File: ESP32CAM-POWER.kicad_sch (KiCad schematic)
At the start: 13 parts, among them J1 Conn_01x02_Female, J2 Conn_01x06_Male, U1 D-SUN-MP1584EN, U2 ESP32-CAM

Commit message: some chages for V1.3
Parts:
- added C1: 100nF, Capacitor_SMD:C_0603_1608Metric, symbol Device:C
- added D3: BZV55C5V1, Diode_SMD:D_MiniMELF, symbol Diode:BZV55C5V1
- added D5, D6, D7, D8: WS2812B, LED_SMD:LED_WS2812B_PLCC4_5.0x5.0mm_P3.2mm, symbol LED:WS2812B
- added J3: Conn_01x02_Male, Jumper:SolderJumper-2_P1.3mm_Open_RoundedPad1.0x1.5mm, symbol Connector:Conn_01x02_Male
- added R3: 10k, Resistor_SMD:R_0603_1608Metric, symbol Device:R
- added SW1: BOOT, Button_Switch_SMD:SW_Push_1P1T_NO_6x6mm_H9.5mm, symbol Switch:SW_SPST
- renumbered D2 to D1, D3 to D2, D1 to D4
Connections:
- net +5V: now also D3.1 (K), D5.1 (VDD), D6.1 (VDD), D7.1 (VDD), D8.1 (VDD), J3.2 (Pin_2); no longer U1.7 (VOUT+), U1.8 (VOUT+)
- net BOOT: now also C1.1, R3.2, SW1.2 (B); no longer J2.6 (Pin_6)
- net GND: now also J2.1 (Pin_1), C1.2, D3.2 (A), D5.3 (VSS), D6.3 (VSS), D7.3 (VSS), D8.3 (VSS), SW1.1 (A); no longer J2.4 (Pin_4), J2.5 (Pin_5)
- net RX: now also J2.4 (Pin_4); no longer J2.3 (Pin_3)
- net TX: now also J2.5 (Pin_5); no longer J2.2 (Pin_2)
- net at D4.2 (A): now also J2.3 (Pin_3); no longer J2.1 (Pin_1)
- net LED: now reaches U2.3 (IO12)
- net LED: now also D5.4 (DIN)
- net +3V3: now reaches U2.9 (3V3)
- net +3V3: now also R3.1
- new net: D6.2 (DOUT), D7.4 (DIN)
- new net: D5.2 (DOUT), D6.4 (DIN)
- new net: J3.1 (Pin_1), U1.7 (VOUT+), U1.8 (VOUT+)
- new net: D7.2 (DOUT), D8.4 (DIN)
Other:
- note added: "Adafruit FTDI Cable https://cdn-shop.adafruit.com/datasheets/FT232_Model.pdf 1: GND 2: CTS 3: 5V 4: TXD 3.3V 5: RXD 3.3V 6: RTS"
- note added: "https://raw.githubusercontent.com/SeeedDocument/forum_doc/master/reg/ESP32_CAM_V1.6.pdf"
- moved on the sheet: U2

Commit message: serveral changes, add USB, still a bit messy
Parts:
- removed C1: 100nF, Capacitor_SMD:C_0603_1608Metric, symbol Device:C
- removed D3: BZV55C5V1, Diode_SMD:D_MiniMELF, symbol Diode:BZV55C5V1
- removed D4: 1N4148WS, Diode_SMD:D_SOD-323, symbol Diode:1N4148WS
- removed J2: Conn_01x06_Male, Connector_PinHeader_2.54mm:PinHeader_1x06_P2.54mm_Horizontal, symbol Connector:Conn_01x06_Male
- removed J3: Conn_01x02_Male, Jumper:SolderJumper-2_P1.3mm_Open_RoundedPad1.0x1.5mm, symbol Connector:Conn_01x02_Male
- removed SW1: BOOT, Button_Switch_SMD:SW_Push_1P1T_NO_6x6mm_H9.5mm, symbol Switch:SW_SPST
- added C1, C2: 1uF, Capacitor_SMD:C_0603_1608Metric, symbol Device:C_Small
- added C3, C4: 20pF, Capacitor_SMD:C_0603_1608Metric, symbol Device:C_Small
- added D10, D9: 1N4148WS, Diode_SMD:D_SOD-323, symbol Diode:1N4148WS
- added D3: LED_O, LED_SMD:LED_0603_1608Metric, symbol Device:LED
- added D4: SN4001W, Diode_SMD:D_SOD-123, symbol Diode:SM4001
- added J2: USB_B_Micro, Connector_USB:USB_Micro-B_Amphenol_10118194_Horizontal, symbol Connector:USB_B_Micro
- added SW1: RESET, bouni:TS-1187A-B-A-B, symbol Switch:SW_DPST
- added SW2: BOOT, bouni:TS-1187A-B-A-B, symbol Switch:SW_DPST
- added TP1, TP2, TP3, TP4: TestPoint, TestPoint:TestPoint_Pad_D1.5mm, symbol Connector:TestPoint
- added U3: ME6206A33XG, Package_TO_SOT_SMD:SOT-23, symbol Regulator_Linear:LM3480-3.3
- added U4: CH340G, Package_SO:SOIC-16_3.9x9.9mm_P1.27mm, symbol Interface_USB:CH340G
- added Y1: 12Mhz, Crystal:Crystal_SMD_3225-4Pin_3.2x2.5mm, symbol Device:Crystal_GND24_Small
- D5, D6, D7, D8, H1, H2, H3, H4, U1, U2: now left out of the parts list
- J1: footprint Connector_Phoenix_MSTB:PhoenixContact_MSTBVA_2,5_2-G-5,08_1x02_P5.08mm_Vertical -> TerminalBlock_RND:TerminalBlock_RND_205-00232_1x02_P5.08mm_Horizontal; now left out of the parts list
- R2, R3: value 10k -> 680
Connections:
- net +3V3: now also C2.1, TP4.1, U3.1 (VO), U4.16 (VCC), U4.4 (V3); no longer R3.1, U2.9 (3V3)
- net +5V: now also U1.4 (VOUT+), D4.1 (K), TP3.1
- net BOOT: now also D10.2 (A), SW2.2; no longer R3.2
- net GND: now also U1.3 (VOUT-), C1.2, C2.2, C3.2, C4.2, D3.1 (K), J2.5 (GND), J2.6 (Shield), SW1.1, SW2.1, TP1.1, U3.3 (GND), U4.1 (GND), Y1.2, Y1.4; no longer U1.2 (VIN-), U1.5 (VOUT-), U1.6 (VOUT-), U2.16 (GND)
- net RX: now also U4.2 (TXD)
- net TX: now also U4.3 (RXD)
- net VCC: now also U1.2 (VIN+); no longer U1.3 (VIN+), U1.4 (VIN+)
- new net: D3.2 (A), R3.2
- new net: C3.1, U4.7 (XI), Y1.3
- new net: C4.1, U4.8 (XO), Y1.1
- new net D+: J2.3 (D+), U4.5 (UD+)
- new net D-: J2.2 (D-), U4.6 (UD-)
- new net DTR: D10.1 (K), U4.13 (~{DTR})
- new net RESET: D9.2 (A), SW1.2, U2.16 (RST)
- new net RTS: D9.1 (K), U4.14 (~{RTS})
- new net VSS: C1.1, D4.2 (A), J2.1 (VBUS), R3.1, TP2.1, U3.2 (VI)
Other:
- note removed: "Adafruit FTDI Cable https://cdn-shop.adafruit.com/datasheets/FT232_Model.pdf 1: GND 2: CTS 3: 5V 4: TXD 3.3V 5: RXD 3.3V 6: RTS"
- moved on the sheet: D1, D2, D5, D6, D7, D8, J1, R1, R2, U2

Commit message: minor cleanups
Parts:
- added TP5: TestPoint, TestPoint:TestPoint_Pad_D1.5mm, symbol Connector:TestPoint
- D3: value LED_O -> LED_B
- renumbered D4 to D11
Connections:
- net VCC: now also TP5.1
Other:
- moved on the sheet: D3, R3, TP1, TP2, TP3, TP4

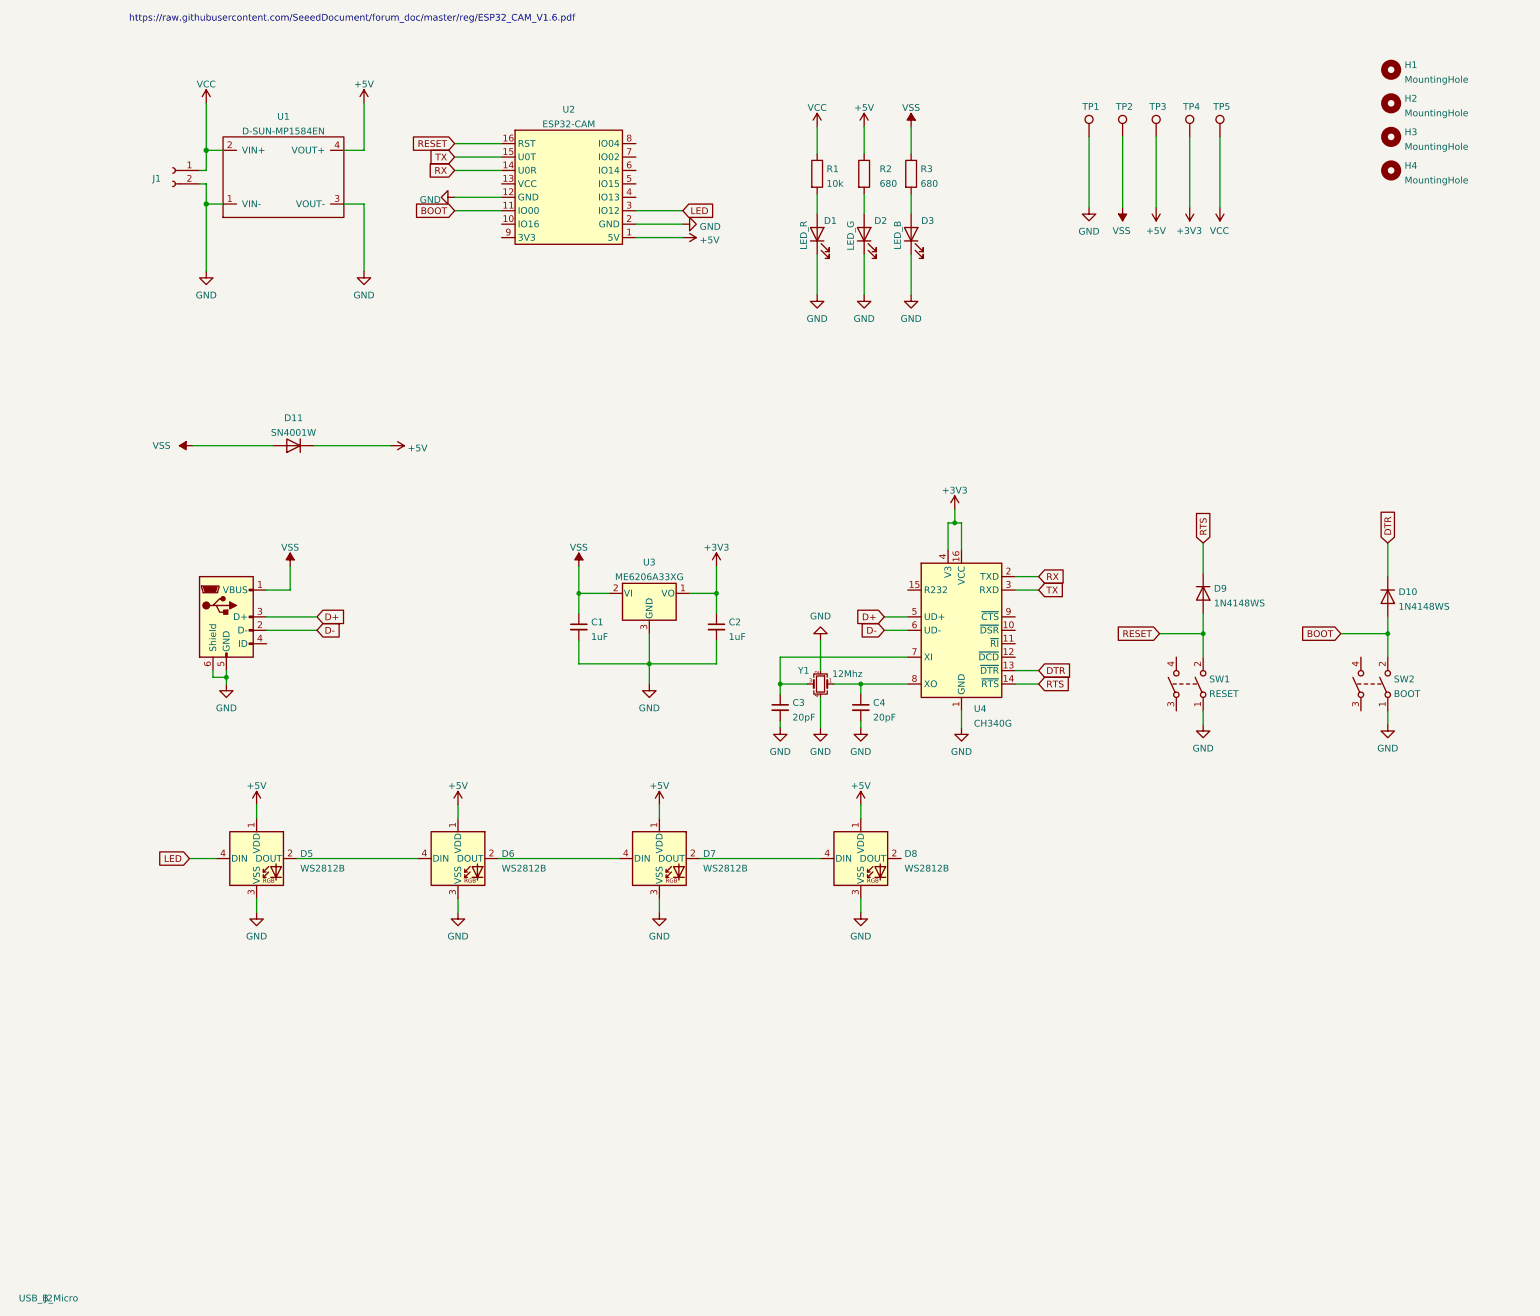
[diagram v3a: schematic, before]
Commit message: massiv rework, mostly simplified the project
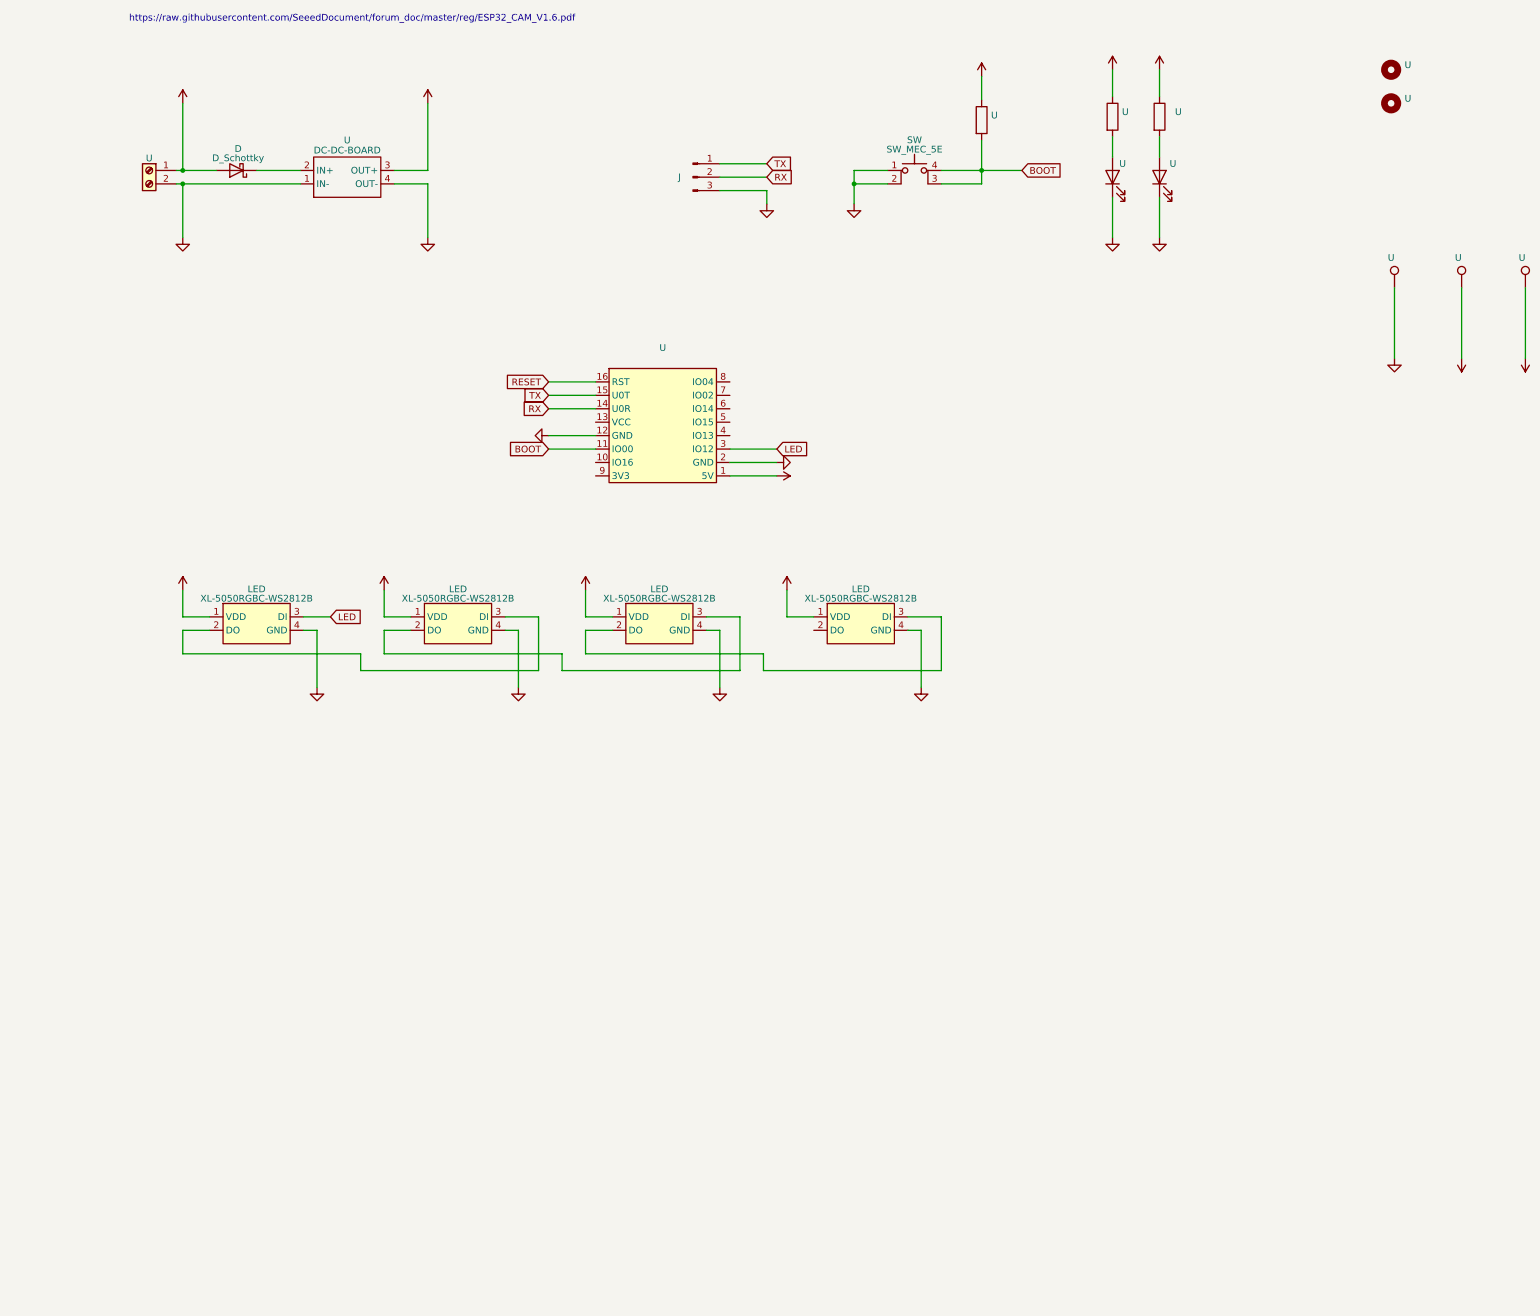
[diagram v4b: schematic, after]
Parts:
- removed C1, C2: 1uF, Capacitor_SMD:C_0603_1608Metric, symbol Device:C_Small
- removed C3, C4: 20pF, Capacitor_SMD:C_0603_1608Metric, symbol Device:C_Small
- removed D10, D9: 1N4148WS, Diode_SMD:D_SOD-323, symbol Diode:1N4148WS
- removed D11: SN4001W, Diode_SMD:D_SOD-123, symbol Diode:SM4001
- removed D3: LED_B, LED_SMD:LED_0603_1608Metric, symbol Device:LED
- removed D5, D6, D7, D8: WS2812B, LED_SMD:LED_WS2812B_PLCC4_5.0x5.0mm_P3.2mm, symbol LED:WS2812B
- removed H3, H4: MountingHole, MountingHole:MountingHole_3.2mm_M3_ISO14580, symbol Mechanical:MountingHole
- removed J1: Conn_01x02_Female, TerminalBlock_RND:TerminalBlock_RND_205-00232_1x02_P5.08mm_Horizontal, symbol Connector:Conn_01x02_Female
- removed J2: USB_B_Micro, Connector_USB:USB_Micro-B_Amphenol_10118194_Horizontal, symbol Connector:USB_B_Micro
- removed R3: 680, Resistor_SMD:R_0603_1608Metric, symbol Device:R
- removed SW1: RESET, bouni:TS-1187A-B-A-B, symbol Switch:SW_DPST
- removed SW2: BOOT, bouni:TS-1187A-B-A-B, symbol Switch:SW_DPST
- removed TP2, TP4: TestPoint, TestPoint:TestPoint_Pad_D1.5mm, symbol Connector:TestPoint
- removed U1: D-SUN-MP1584EN, bouni:D-SUN-MP1584EN, symbol bouni:D-SUN-MP1584EN
- removed U3: ME6206A33XG, Package_TO_SOT_SMD:SOT-23, symbol Regulator_Linear:LM3480-3.3
- removed U4: CH340G, Package_SO:SOIC-16_3.9x9.9mm_P1.27mm, symbol Interface_USB:CH340G
- removed Y1: 12Mhz, Crystal:Crystal_SMD_3225-4Pin_3.2x2.5mm, symbol Device:Crystal_GND24_Small
- added D: D_Schottky, symbol Device:D_Schottky
- added J: Conn_01x03_Male, symbol Connector:Conn_01x03_Male
- added LED (x4): XL-5050RGBC-WS2812B, LED-SMD_4P-L5.0-W5.0-BL_XL-5050RGBC, symbol LCSC:XL-5050RGBC-WS2812B
- added SW: SW_MEC_5E, symbol Switch:SW_MEC_5E
- added U: (no value), symbol Device:R
- added U: (no value), symbol Connector:Screw_Terminal_01x02
- added U: DC-DC-BOARD, symbol bouni:DC-DC-BOARD
- U: renamed from R2; value 680 -> (none); footprint Resistor_SMD:R_0603_1608Metric -> (none); LCSC (none) -> C23228
- U: renamed from H2; value MountingHole -> (none); footprint MountingHole:MountingHole_3.2mm_M3_ISO14580 -> (none)
- U: renamed from D1; value LED_R -> (none); footprint LED_SMD:LED_0603_1608Metric -> (none); LCSC (none) -> C72038
- U: renamed from R1; value 10k -> (none); footprint Resistor_SMD:R_0603_1608Metric -> (none); LCSC (none) -> C25804
- U: renamed from TP5; value TestPoint -> (none); footprint TestPoint:TestPoint_Pad_D1.5mm -> (none)
- U: renamed from TP3; value TestPoint -> (none); footprint TestPoint:TestPoint_Pad_D1.5mm -> (none)
- U: renamed from U2; value ESP32-CAM -> (none); footprint bouni:ESP32-CAM -> (none)
- U: renamed from TP1; value TestPoint -> (none); footprint TestPoint:TestPoint_Pad_D1.5mm -> (none)
- U: renamed from H1; value MountingHole -> (none); footprint MountingHole:MountingHole_3.2mm_M3_ISO14580 -> (none)
- U: renamed from D2; value LED_G -> (none); footprint LED_SMD:LED_0603_1608Metric -> (none); LCSC (none) -> C72043
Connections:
- net +5V: now also LED.1 (VDD), LED.1 (VDD), LED.1 (VDD), LED.1 (VDD), U.1, U.3 (OUT+)
- net BOOT: now also SW.3 (K), SW.4 (A), U.2
- net GND: now also J.3 (Pin_3), LED.4 (GND), LED.4 (GND), LED.4 (GND), LED.4 (GND), SW.1, SW.2, U.1 (IN-), U.2 (Pin_2), U.4 (OUT-)
- net LED: now also LED.3 (DI)
- net RX: now also J.2 (Pin_2)
- net TX: now also J.1 (Pin_1)
- net VCC: now also D.2 (A), U.1 (Pin_1)
- new net: LED.2 (DO), LED.3 (DI) (x3)
- new net: D.1 (K), U.2 (IN+)
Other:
- moved on the sheet: U

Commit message: Add notes to schematic
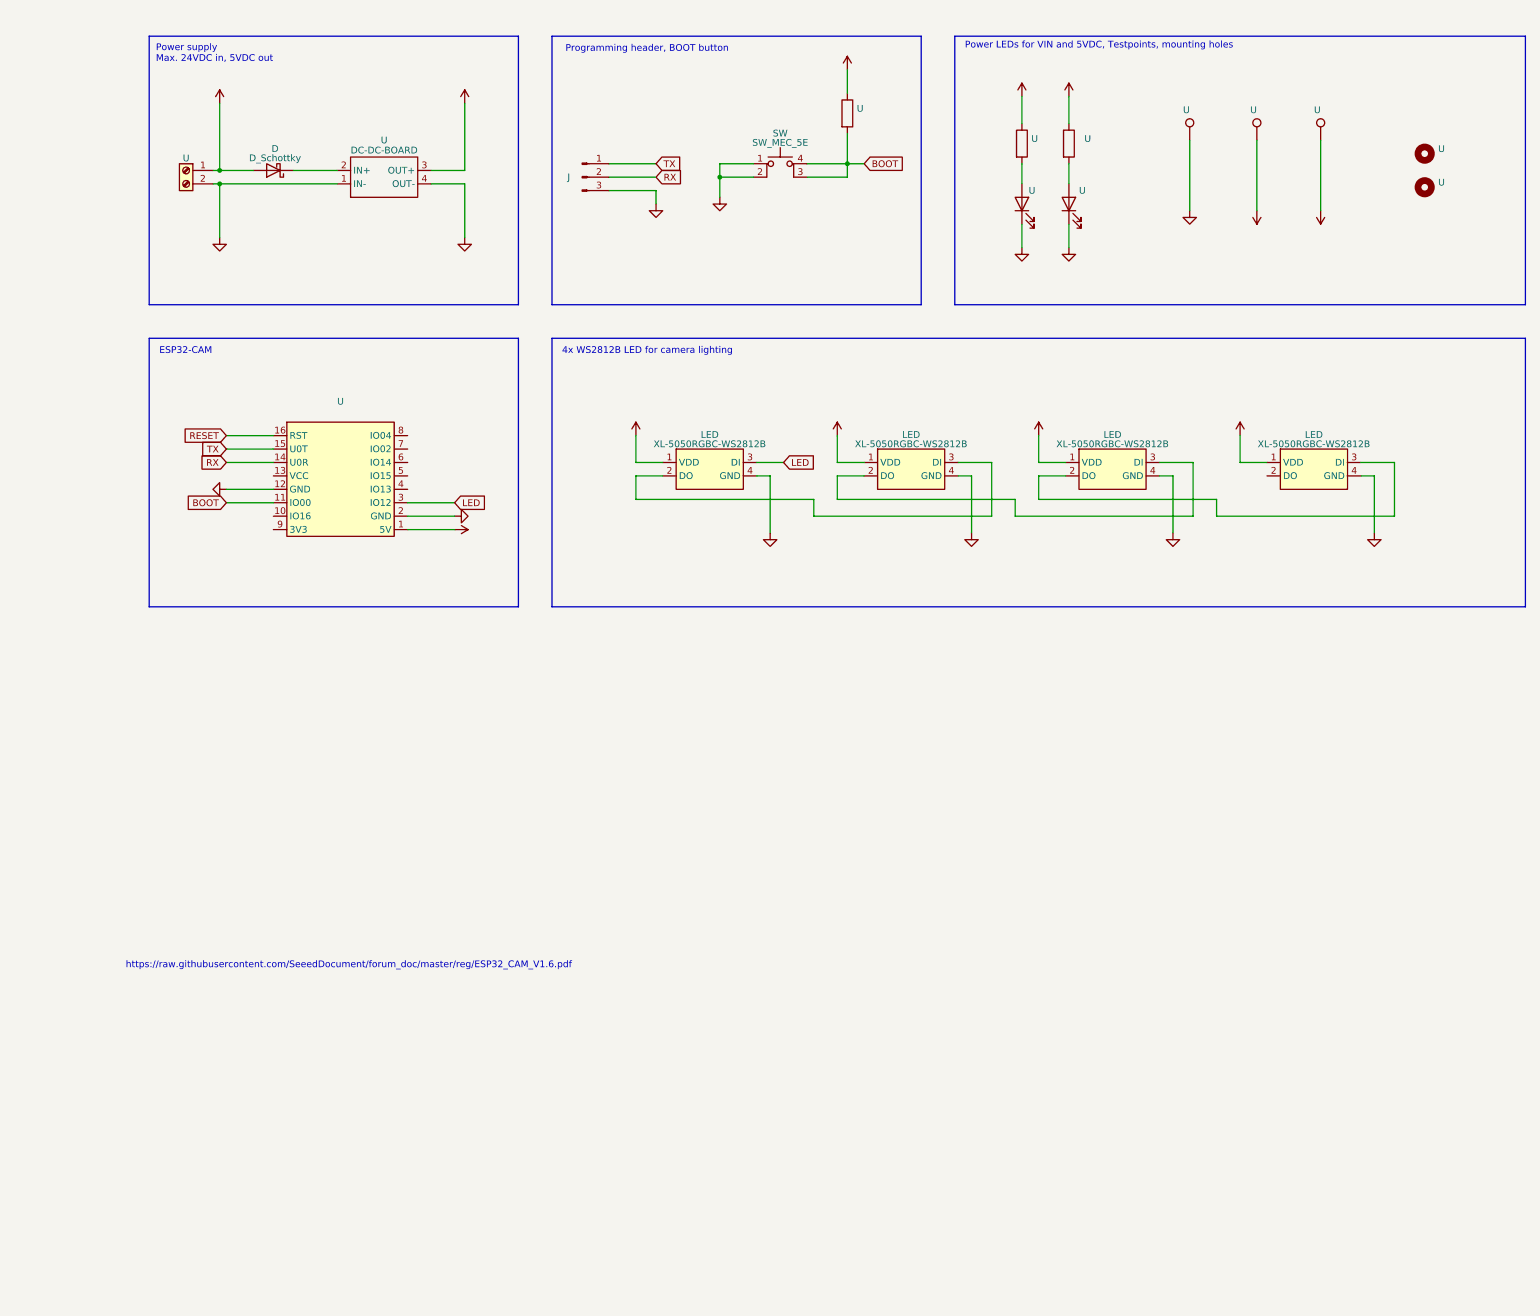
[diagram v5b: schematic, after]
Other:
- note added: "4x WS2812B LED for camera lighting"
- note added: "ESP32-CAM"
- note added: "Power LEDs for VIN and 5VDC, Testpoints, mounting holes"
- note added: "Power supply Max. 24VDC in, 5VDC out"
- note added: "Programming header, BOOT button"
- company: (none) -> Bouni, 2022
- title: (none) -> ESP32-CAM POWER BOARD
- moved on the sheet: D, J, LED, SW, U
